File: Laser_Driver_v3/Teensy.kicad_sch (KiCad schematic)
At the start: 1 part

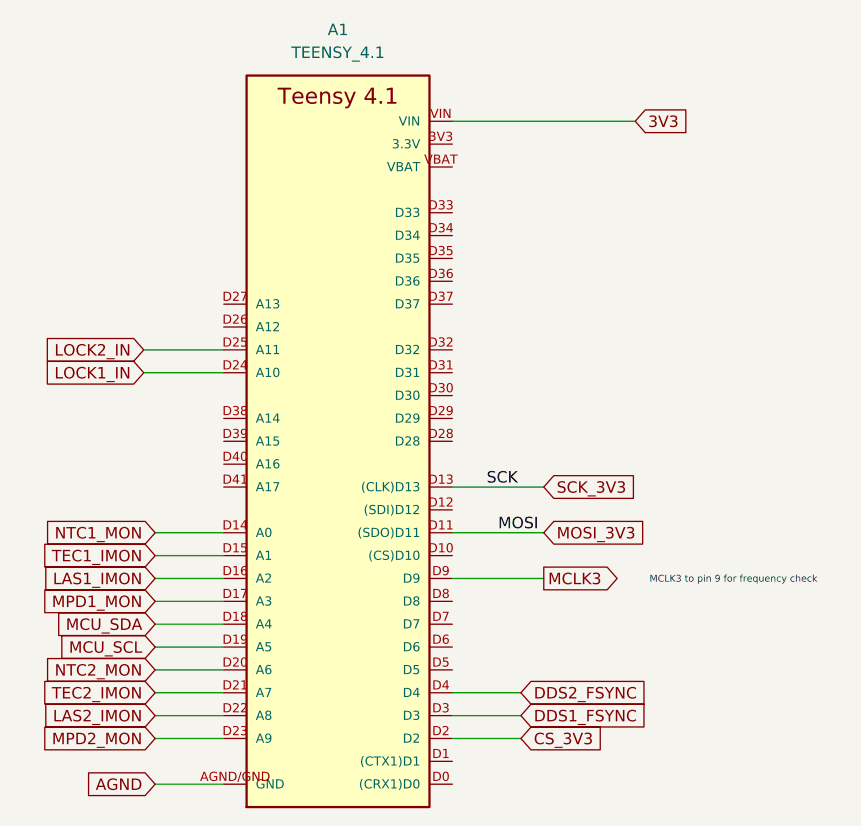
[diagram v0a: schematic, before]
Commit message: Clearing ERC errors. laying out components.
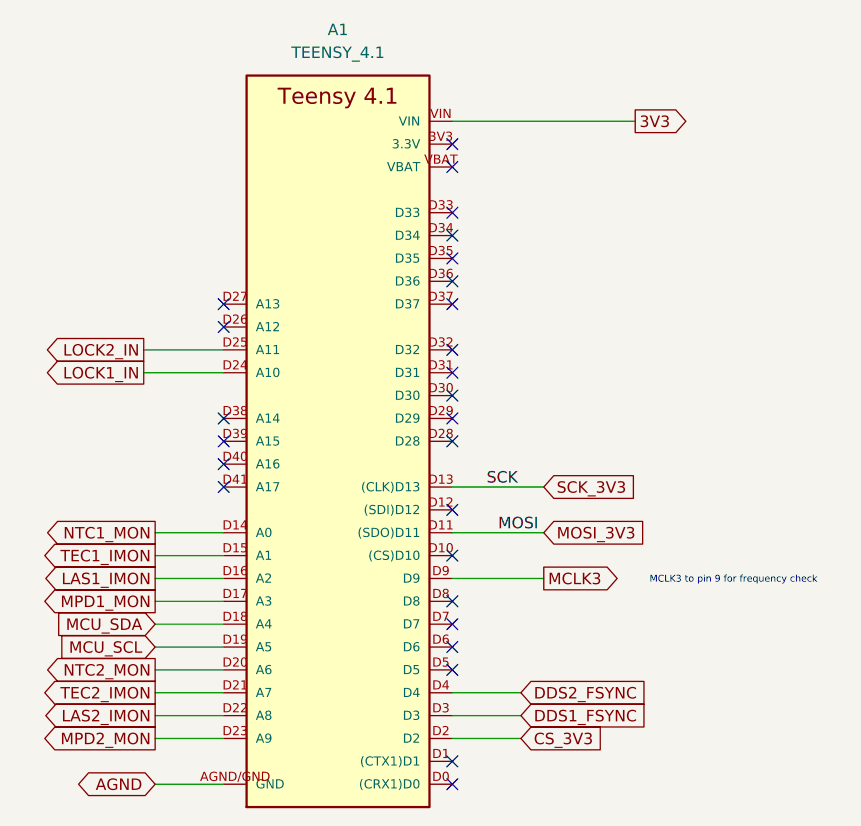
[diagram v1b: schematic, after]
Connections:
- no-connect marks 0 -> 26
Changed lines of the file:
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@@
 		)
 	)
+	(no_connect
+		(at 116.84 64.77)
+	)
+	(no_connect
+		(at 116.84 54.61)
+	)
+	(no_connect
+		(at 116.84 72.39)
+	)
+	(no_connect
+		(at 91.44 67.31)
+	)
+	(no_connect
+		(at 116.84 46.99)
+	)
+	(no_connect
+		(at 116.84 102.87)
+	)
+	(no_connect
+		(at 116.84 105.41)
+	)
+	(no_connect
+		(at 116.84 100.33)
+	)
+	(no_connect
+		(at 116.84 118.11)
+	)
+	(no_connect
+		(at 116.84 97.79)
+	)
+	(no_connect
+		(at 116.84 69.85)
+	)
+	(no_connect
+		(at 116.84 115.57)
+	)
+	(no_connect
+		(at 116.84 74.93)
+	)
+	(no_connect
+		(at 116.84 80.01)
+	)
+	(no_connect
+		(at 116.84 92.71)
+	)
+	(no_connect
+		(at 91.44 82.55)
+	)
+	(no_connect
+		(at 116.84 62.23)
+	)
+	(no_connect
+		(at 116.84 59.69)
+	)
+	(no_connect
+		(at 91.44 77.47)
+	)
+	(no_connect
+		(at 116.84 87.63)
+	)
+	(no_connect
+		(at 91.44 80.01)
+	)
+	(no_connect
+		(at 116.84 49.53)
+	)
+	(no_connect
+		(at 116.84 77.47)
+	)
+	(no_connect
+		(at 91.44 64.77)
+	)
+	(no_connect
+		(at 91.44 85.09)
+	)
+	(no_connect
+		(at 116.84 57.15)
+	)
 	(wire
 		(pts
@@
 	)
 	(global_label "TEC2_IMON"
-		(shape input)
+		(shape output)
 		(at 83.82 107.95 180)
 		(fields_autoplaced yes)
@@
 		)
 		(property "Intersheetrefs" "${INTERSHEET_REFS}"
-			(at 83.82 107.95 0)
+			(at 70.5539 107.95 0)
 			(hide yes)
 			(show_name no)
@@
 	)
 	(global_label "MPD1_MON"
-		(shape input)
+		(shape output)
 		(at 83.82 97.79 180)
 		(fields_autoplaced yes)
@@
 		)
 		(property "Intersheetrefs" "${INTERSHEET_REFS}"
-			(at 83.82 97.79 0)
+			(at 70.5539 97.79 0)
 			(hide yes)
 			(show_name no)
@@
 	)
 	(global_label "TEC1_IMON"
-		(shape input)
+		(shape output)
 		(at 83.82 92.71 180)
 		(fields_autoplaced yes)
@@
 		)
 		(property "Intersheetrefs" "${INTERSHEET_REFS}"
-			(at 83.82 92.71 0)
+			(at 70.5539 92.71 0)
 			(hide yes)
 			(show_name no)
@@
 		)
 		(property "Intersheetrefs" "${INTERSHEET_REFS}"
-			(at 124.46 107.95 0)
+			(at 139.359 107.95 0)
 			(hide yes)
 			(show_name no)
@@
 	)
 	(global_label "NTC1_MON"
-		(shape input)
+		(shape output)
 		(at 83.82 90.17 180)
 		(fields_autoplaced yes)
@@
 		)
 		(property "Intersheetrefs" "${INTERSHEET_REFS}"
-			(at 83.82 90.17 0)
+			(at 70.9772 90.17 0)
 			(hide yes)
 			(show_name no)
@@
 	)
 	(global_label "LAS2_IMON"
-		(shape input)
+		(shape output)
 		(at 83.82 110.49 180)
 		(fields_autoplaced yes)
@@
 		)
 		(property "Intersheetrefs" "${INTERSHEET_REFS}"
-			(at 83.82 110.49 0)
+			(at 70.6143 110.49 0)
 			(hide yes)
 			(show_name no)
@@
 	)
 	(global_label "AGND"
-		(shape input)
+		(shape bidirectional)
 		(at 83.82 118.11 180)
 		(fields_autoplaced yes)
@@
 		)
 		(property "Intersheetrefs" "${INTERSHEET_REFS}"
-			(at 83.82 118.11 0)
+			(at 74.7644 118.11 0)
 			(hide yes)
 			(show_name no)
@@
 	)
 	(global_label "LOCK2_IN"
-		(shape input)
+		(shape output)
 		(at 82.55 69.85 180)
 		(fields_autoplaced yes)
@@
 		)
 		(property "Intersheetrefs" "${INTERSHEET_REFS}"
-			(at 82.55 69.85 0)
+			(at 70.5538 69.85 0)
 			(hide yes)
 			(show_name no)
@@
 	)
 	(global_label "NTC2_MON"
-		(shape input)
+		(shape output)
 		(at 83.82 105.41 180)
 		(fields_autoplaced yes)
@@
 		)
 		(property "Intersheetrefs" "${INTERSHEET_REFS}"
-			(at 83.82 105.41 0)
+			(at 70.9772 105.41 0)
 			(hide yes)
 			(show_name no)
@@
 	)
 	(global_label "3V3"
-		(shape input)
+		(shape output)
 		(at 137.16 44.45 0)
 		(fields_autoplaced yes)
@@
 	)
 	(global_label "MPD2_MON"
-		(shape input)
+		(shape output)
 		(at 83.82 113.03 180)
 		(fields_autoplaced yes)
@@
 		)
 		(property "Intersheetrefs" "${INTERSHEET_REFS}"
-			(at 83.82 113.03 0)
+			(at 70.5539 113.03 0)
 			(hide yes)
 			(show_name no)
@@
 	)
 	(global_label "LAS1_IMON"
-		(shape input)
+		(shape output)
 		(at 83.82 95.25 180)
 		(fields_autoplaced yes)
@@
 		)
 		(property "Intersheetrefs" "${INTERSHEET_REFS}"
-			(at 83.82 95.25 0)
+			(at 70.6143 95.25 0)
 			(hide yes)
 			(show_name no)
@@
 	)
 	(global_label "LOCK1_IN"
-		(shape input)
+		(shape output)
 		(at 82.55 72.39 180)
 		(fields_autoplaced yes)
@@
 		)
 		(property "Intersheetrefs" "${INTERSHEET_REFS}"
-			(at 82.55 72.39 0)
+			(at 70.5538 72.39 0)
 			(hide yes)
 			(show_name no)

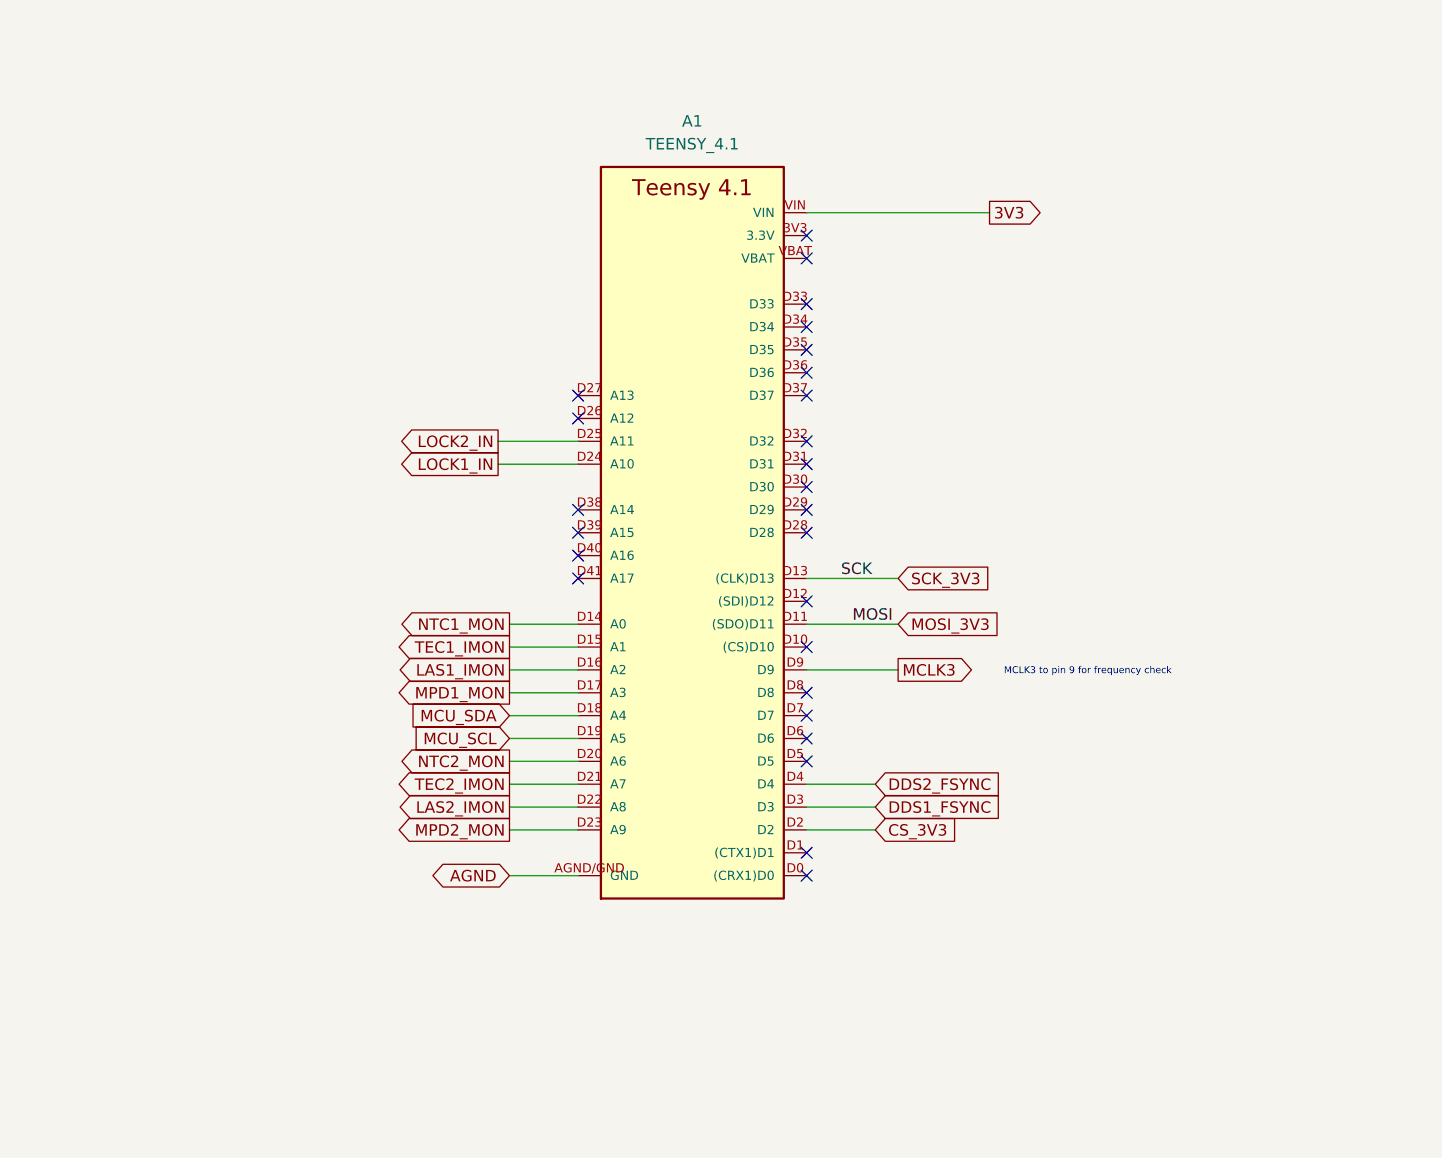
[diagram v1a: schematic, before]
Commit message: Added display to schematic.  Updated BOM.
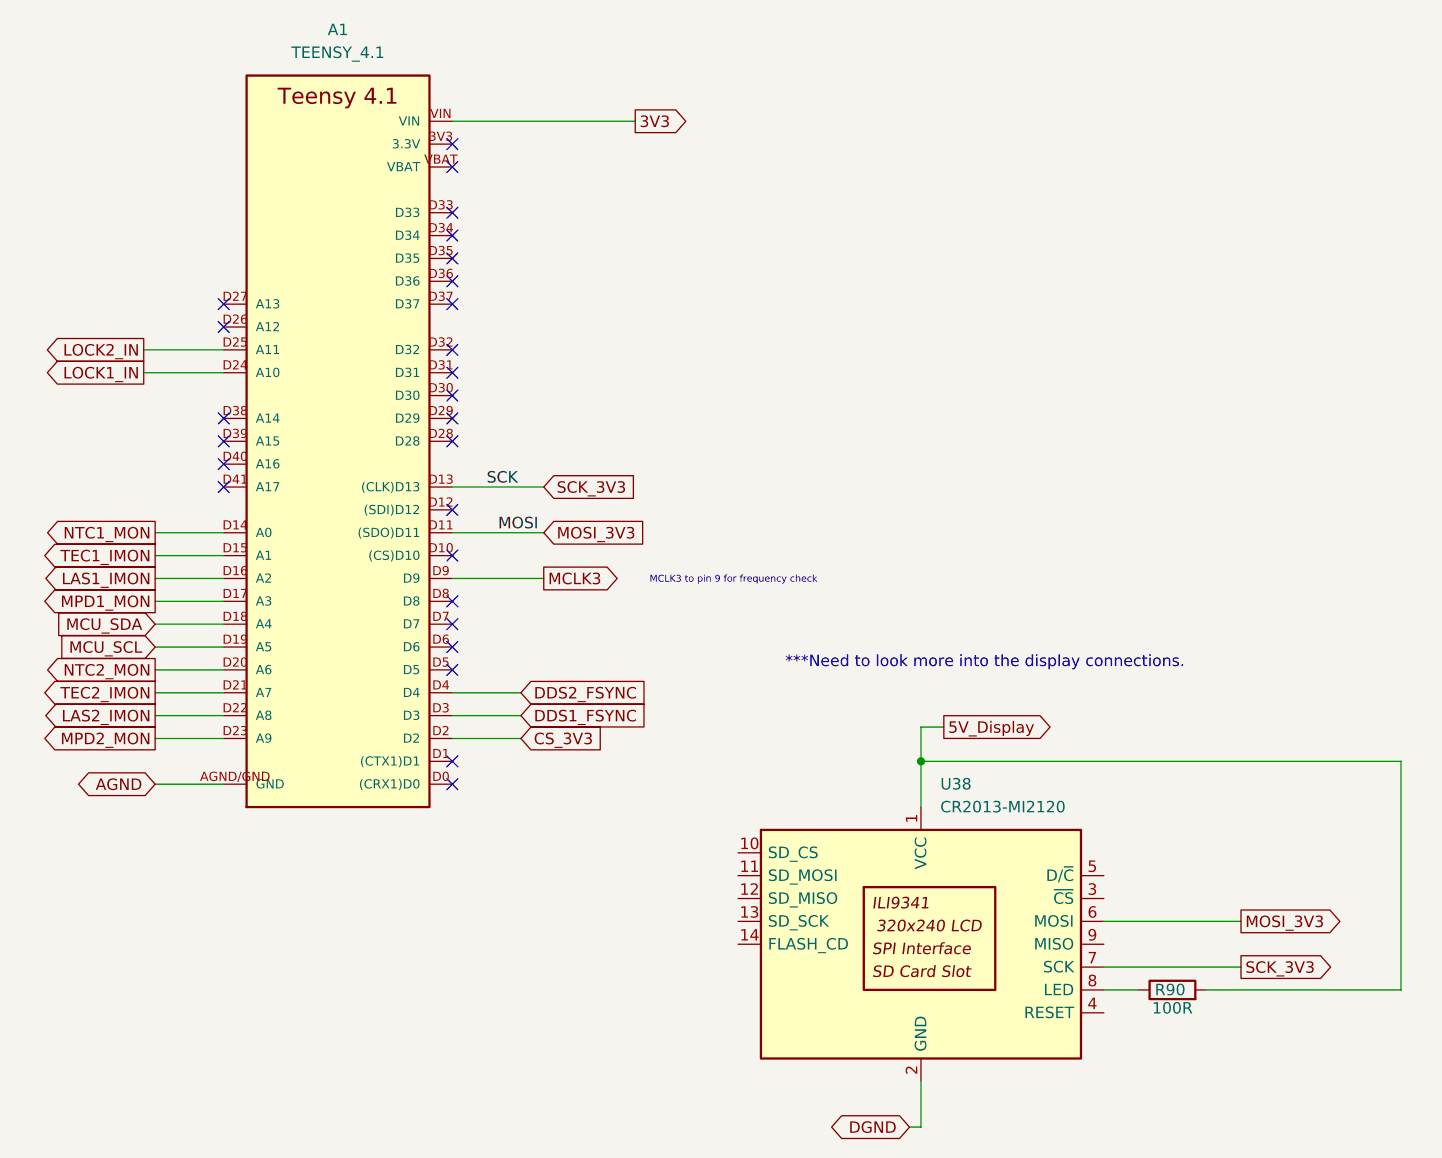
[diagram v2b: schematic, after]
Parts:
- added R90: 100R, symbol Device:R
- added U38: CR2013-MI2120, Display:CR2013-MI2120, symbol Driver_Display:CR2013-MI2120
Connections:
- net MOSI_3V3: now also U38.6 (MOSI)
- net SCK_3V3: now also U38.7 (SCK)
- new net: R90.1, U38.8 (LED)
- new net 5V_Display: R90.2, U38.1 (VCC)
- new net DGND: U38.2 (GND)
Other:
- note added: "***Need to look more into the display connections."
- moved on the sheet: A1

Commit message: Update to teensy pinout and config. Working on PCB
Improved pin selection on Teensy for better operation.
Started working through the PCB from in the power input.
Updating footprints and getting the layout organized.
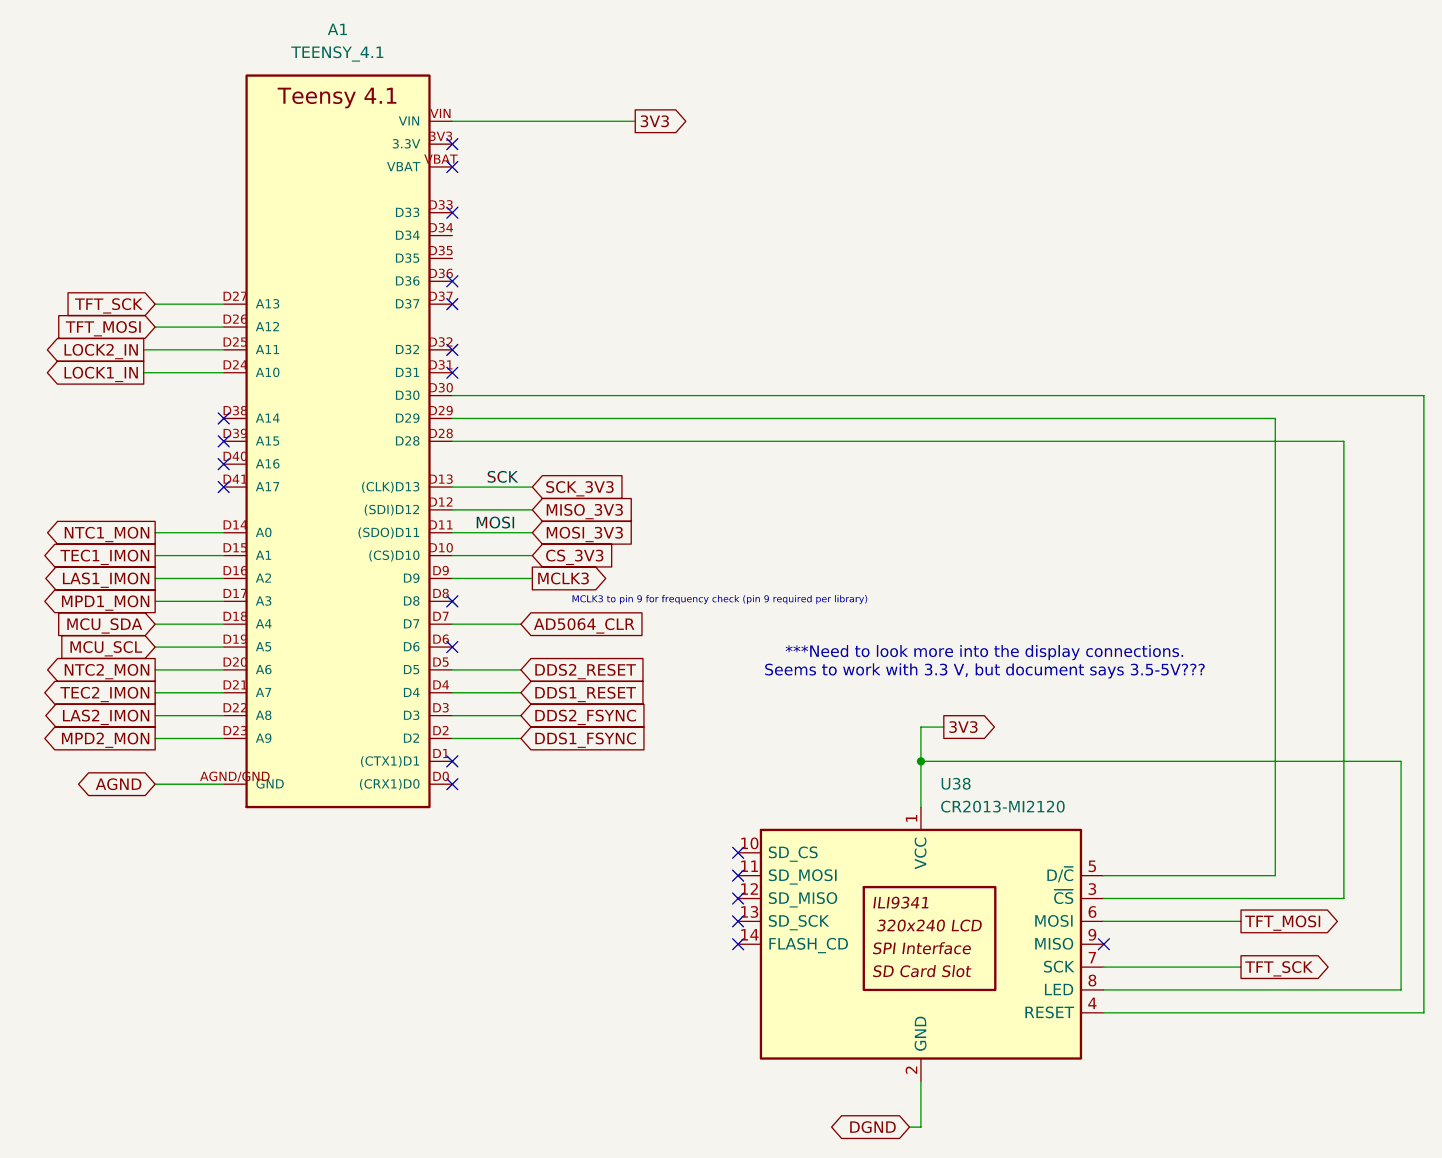
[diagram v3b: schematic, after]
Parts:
- removed R90: 100R, symbol Device:R
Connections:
- net 5V_Display is gone; now on net 3V3: U38.1 (VCC)
- net 3V3: now also U38.8 (LED)
- net CS_3V3: now also A1.D10 ((CS)D10); no longer A1.D2
- net DDS1_FSYNC: now also A1.D2; no longer A1.D3
- net DDS2_FSYNC: now also A1.D3; no longer A1.D4
- net MOSI_3V3: no longer U38.6 (MOSI)
- net SCK_3V3: no longer U38.7 (SCK)
- net MISO_3V3: now reaches A1.D12 ((SDI)D12)
- net TFT_MOSI: now reaches A1.D26 (A12)
- net TFT_MOSI: now also U38.6 (MOSI)
- net TFT_SCK: now reaches A1.D27 (A13)
- net TFT_SCK: now also U38.7 (SCK)
- net at A1.D28: now also U38.3 (~{CS})
- net at A1.D29: now also U38.5 (D/~{C})
- net at A1.D30: now also U38.4 (RESET)
- net DDS2_RESET: now reaches A1.D5
- net AD5064_CLR: now reaches A1.D7
- new net DDS1_RESET: A1.D4
- no-connect marks 26 -> 21
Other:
- note added: "***Need to look more into the display connections. Seems to work with 3.3 V, but document says 3.5-5V???"
- note added: "MCLK3 to pin 9 for frequency check (pin 9 required per library)"
- note removed: "***Need to look more into the display connections."
- note removed: "MCLK3 to pin 9 for frequency check"

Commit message: Added separate xfrmer for 6V.
Added inrush protection with NTC and increased capacitance to reduce ripple on 6V
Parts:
- renumbered U38 to U37
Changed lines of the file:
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@@
 		(dnp no)
 		(fields_autoplaced yes)
-		(property "Reference" "U38"
+		(property "Reference" "U37"
 			(at 131.6833 107.95 0)
 			(show_name no)
@@
 			(project "laser_driver_v3"
 				(path "/b2c3d4e5-f6a7-8901-bcde-f12345678901/20b1c7a7-d05f-4e99-ab1a-7c26c0a8ad66"
-					(reference "U38")
+					(reference "U37")
 					(unit 1)
 				)
